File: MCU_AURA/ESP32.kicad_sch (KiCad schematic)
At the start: 18 parts, among them J200 TC2050-IDC-430, U200 ESP32-S3-WROOM-1, U201 USBLC6-2SC6

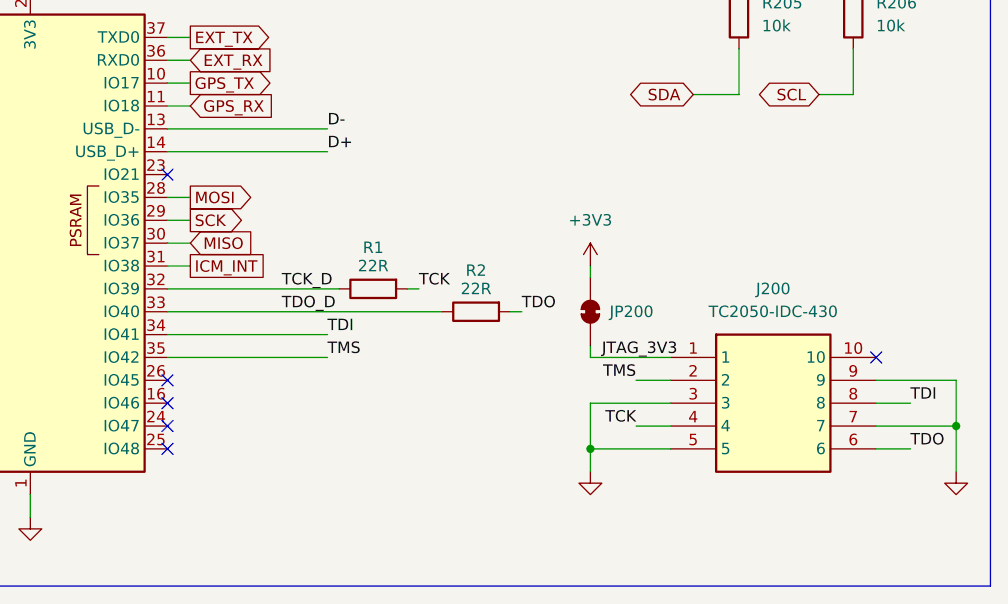
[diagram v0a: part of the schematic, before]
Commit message: Replaced JTAG with Flash
JTAG is used through USB so a Flash chip was added to MCU. PDB is just being cleaned up currently.
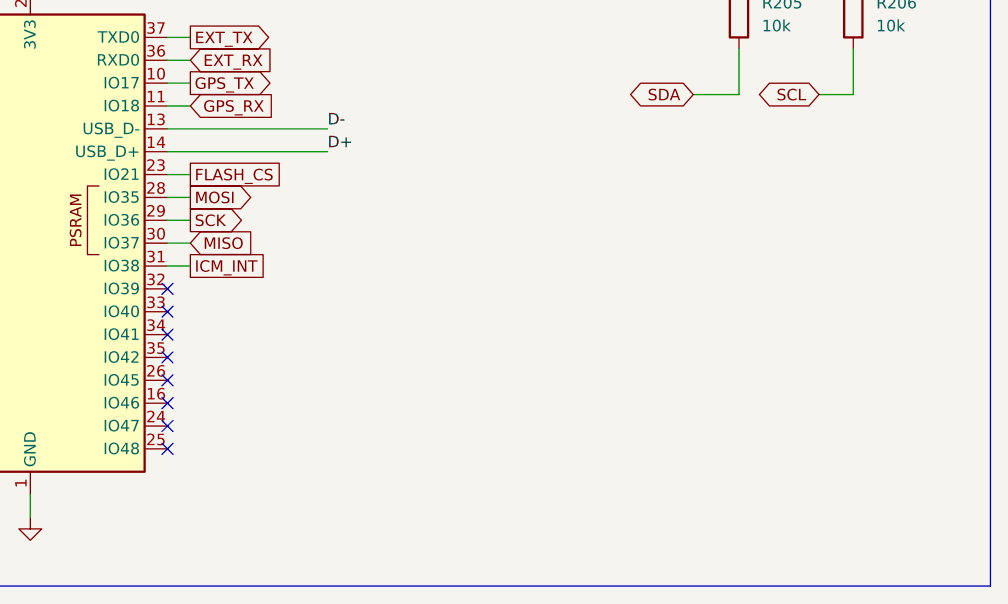
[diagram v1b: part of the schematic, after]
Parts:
- removed J200: TC2050-IDC-430, TC2050-IDC:TC2050-IDC, symbol TC2050-IDC:TC2050-IDC-430
- removed JP200: SolderJumper_2_Bridged, Jumper:SolderJumper-2_P1.3mm_Open_RoundedPad1.0x1.5mm, symbol Jumper:SolderJumper_2_Bridged
- removed R1, R2: 22R, Resistor_SMD:R_0402_1005Metric, symbol Device:R
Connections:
- net FLASH_CS: now reaches U200.23 (IO21)
- net TCK_D: no longer names the net of U200.32 (IO39)
- net TDI: no longer names the net of U200.34 (IO41)
- net TDO_D: no longer names the net of U200.33 (IO40)
- net TMS: no longer names the net of U200.35 (IO42)
- no-connect marks 13 -> 15

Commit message: Second Iteration MCU
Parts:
- added C205, C206: 100n, Capacitor_SMD:C_0402_1005Metric, symbol Device:C
- added U202: TCAN1042VDRBRQ1, TCAN1042VDRBRQ1:DRB0008F, symbol TCAN1042VDRBRQ1:TCAN1042VDRBRQ1
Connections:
- net +3V3: now also C206.1, U202.5 (VIO)
- net GND: now also C205.2, C206.2, U202.2 (GND), U202.9 (PAD)
- net CAN_RX: now reaches U200.24 (IO47)
- net CAN_RX: now also U202.4 (RXD)
- net CAN_TX: now reaches U200.25 (IO48)
- net CAN_TX: now also U202.1 (TXD)
- net CAN_STB: now reaches U200.26 (IO45)
- net CAN_STB: now also U202.8 (STB)
- new net +5V_FILT: C205.1, U202.3 (VCC)
- new net CANH: U202.7 (CANH)
- new net CANL: U202.6 (CANL)
- no-connect marks 15 -> 12
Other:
- moved on the sheet: C200, C201, C202, R200, R205, R206, U200

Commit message: First Order
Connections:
- net GND: now also U202.8 (STB)
- net CAN_STB: no longer names the net of U200.26 (IO45)
- net CAN_STB: no longer U202.8 (STB)
- no-connect marks 12 -> 13
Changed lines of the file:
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@@
 	)
 	(no_connect
+		(at 165.1 115.57)
+	)
+	(no_connect
 		(at 165.1 107.95)
 	)
@@
 	(wire
 		(pts
-			(xy 186.69 118.11) (xy 195.58 118.11)
-		)
-		(stroke
-			(width 0)
-			(type default)
-		)
-	)
-	(wire
-		(pts
 			(xy 111.76 87.63) (xy 111.76 90.17)
 		)
@@
 	(wire
 		(pts
+			(xy 194.31 118.11) (xy 195.58 118.11)
+		)
+		(stroke
+			(width 0)
+			(type default)
+		)
+	)
+	(wire
+		(pts
 			(xy 111.76 77.47) (xy 134.62 77.47)
 		)
@@
 	(wire
 		(pts
-			(xy 222.25 111.76) (xy 227.33 111.76)
+			(xy 194.31 119.38) (xy 194.31 118.11)
 		)
 		(stroke
@@
 	(wire
 		(pts
-			(xy 72.39 76.2) (xy 72.39 78.74)
+			(xy 222.25 111.76) (xy 227.33 111.76)
 		)
 		(stroke
@@
 	(wire
 		(pts
-			(xy 132.08 92.71) (xy 134.62 92.71)
+			(xy 72.39 76.2) (xy 72.39 78.74)
 		)
 		(stroke
@@
 	(wire
 		(pts
-			(xy 67.31 71.12) (xy 64.77 71.12)
+			(xy 132.08 92.71) (xy 134.62 92.71)
 		)
 		(stroke
@@
 	(wire
 		(pts
-			(xy 186.69 114.3) (xy 195.58 114.3)
+			(xy 67.31 71.12) (xy 64.77 71.12)
 		)
 		(stroke
@@
 	(wire
 		(pts
-			(xy 93.98 127) (xy 93.98 116.84)
+			(xy 186.69 114.3) (xy 195.58 114.3)
 		)
 		(stroke
@@
 	(wire
 		(pts
-			(xy 165.1 115.57) (xy 167.64 115.57)
+			(xy 93.98 127) (xy 93.98 116.84)
 		)
 		(stroke
@@
 		)
 	)
-	(label "CAN_STB"
-		(at 186.69 118.11 0)
-		(effects
-			(font
-				(size 1.27 1.27)
-			)
-			(justify left bottom)
-		)
-	)
 	(label "D+"
 		(at 104.14 71.12 0)
@@
 		)
 	)
-	(label "CAN_STB"
-		(at 167.64 115.57 0)
-		(effects
-			(font
-				(size 1.27 1.27)
-			)
-			(justify left bottom)
-		)
-	)
 	(label "USB_MCU_D-"
 		(at 91.44 68.58 180)
@@
 	)
 	(symbol
+		(lib_id "power:GND")
+		(at 194.31 119.38 0)
+		(unit 1)
+		(exclude_from_sim no)
+		(in_bom yes)
+		(on_board yes)
+		(dnp no)
+		(fields_autoplaced yes)
+		(property "Reference" "#PWR066"
+			(at 194.31 125.73 0)
+			(effects
+				(font
+					(size 1.27 1.27)
+				)
+				(hide yes)
+			)
+		)
+		(property "Value" "GND"
+			(at 194.31 124.46 0)
+			(effects
+				(font
+					(size 1.27 1.27)
+				)
+				(hide yes)
+			)
+		)
+		(property "Footprint" ""
+			(at 194.31 119.38 0)
+			(effects
+				(font
+					(size 1.27 1.27)
+				)
+				(hide yes)
+			)
+		)
+		(property "Datasheet" ""
+			(at 194.31 119.38 0)
+			(effects
+				(font
+					(size 1.27 1.27)
+				)
+				(hide yes)
+			)
+		)
+		(property "Description" "Power symbol creates a global label with name \"GND\" , ground"
+			(at 194.31 119.38 0)
+			(effects
+				(font
+					(size 1.27 1.27)
+				)
+				(hide yes)
+			)
+		)
+		(pin "1"
+		)
+		(instances
+			(project "MCU_AURA"
+				(path "/c0b09de1-c640-438f-9ef5-dda14a6aac71/b7286ff6-080d-4fe9-98ea-7dd25e1f4a61"
+					(reference "#PWR066")
+					(unit 1)
+				)
+			)
+		)
+	)
+	(symbol
 		(lib_id "power:+5V")
 		(at 196.85 90.17 0)
@@
 	)
 	(symbol
-		(lib_id "power:GND")
-		(at 207.01 132.08 0)
-		(unit 1)
-		(exclude_from_sim no)
-		(in_bom yes)
-		(on_board yes)
-		(dnp no)
-		(fields_autoplaced yes)
-		(property "Reference" "#PWR066"
-			(at 207.01 138.43 0)
-			(effects
-				(font
-					(size 1.27 1.27)
-				)
-				(hide yes)
-			)
-		)
-		(property "Value" "GND"
-			(at 207.01 137.16 0)
-			(effects
-				(font
-					(size 1.27 1.27)
-				)
-				(hide yes)
-			)
-		)
-		(property "Footprint" ""
-			(at 207.01 132.08 0)
-			(effects
-				(font
-					(size 1.27 1.27)
-				)
-				(hide yes)
-			)
-		)
-		(property "Datasheet" ""
-			(at 207.01 132.08 0)
-			(effects
-				(font
-					(size 1.27 1.27)
-				)
-				(hide yes)
-			)
-		)
-		(property "Description" "Power symbol creates a global label with name \"GND\" , ground"
-			(at 207.01 132.08 0)
-			(effects
-				(font
-					(size 1.27 1.27)
-				)
-				(hide yes)
-			)
-		)
-		(pin "1"
-		)
-		(instances
-			(project "MCU_AURA"
-				(path "/c0b09de1-c640-438f-9ef5-dda14a6aac71/b7286ff6-080d-4fe9-98ea-7dd25e1f4a61"
-					(reference "#PWR066")
-					(unit 1)
-				)
-			)
-		)
-	)
-	(symbol
 		(lib_id "Device:C")
 		(at 196.85 97.79 0)
@@
 					(unit 1)
 				)
+			)
+		)
+	)
+	(symbol
+		(lib_id "power:GND")
+		(at 207.01 132.08 0)
+		(unit 1)
+		(exclude_from_sim no)
+		(in_bom yes)
+		(on_board yes)
+		(dnp no)
+		(fields_autoplaced yes)
+		(property "Reference" "#PWR067"
+			(at 207.01 138.43 0)
+			(effects
+				(font
+					(size 1.27 1.27)
+				)
+				(hide yes)
+			)
+		)
+		(property "Value" "GND"
+			(at 207.01 137.16 0)
+			(effects
+				(font
+					(size 1.27 1.27)
+				)
+				(hide yes)
+			)
+		)
+		(property "Footprint" ""
+			(at 207.01 132.08 0)
+			(effects
+				(font
+					(size 1.27 1.27)
+				)
+				(hide yes)
+			)
+		)
+		(property "Datasheet" ""
+			(at 207.01 132.08 0)
+			(effects
+				(font
+					(size 1.27 1.27)
+				)
+				(hide yes)
+			)
+		)
+		(property "Description" "Power symbol creates a global label with name \"GND\" , ground"
+			(at 207.01 132.08 0)
+			(effects
+				(font
+					(size 1.27 1.27)
+				)
+				(hide yes)
+			)
+		)
+		(pin "1"
+		)
+		(instances
+			(project "MCU_AURA"
+				(path "/c0b09de1-c640-438f-9ef5-dda14a6aac71/b7286ff6-080d-4fe9-98ea-7dd25e1f4a61"
+					(reference "#PWR067")
+					(unit 1)
+				)
